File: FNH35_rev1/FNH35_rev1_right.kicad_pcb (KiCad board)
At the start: 2 copper layers, 126.2 x 116.7 mm, 117 parts, among them IC12 NUF2221W1T2G, J1 Conn_01x03, J2 Conn_01x08, J3 DX07B024JJ3R1600, K201 KEYSW, K202 KEYSW, K203 KEYSW, K204 KEYSW, K205 KEYSW, K206 KEYSW, K207 KEYSW, K208 KEYSW, K209 KEYSW, K210 KEYSW, K211 KEYSW, K212 KEYSW, K213 KEYSW, K214 KEYSW, K215 KEYSW, K216 KEYSW, K217 KEYSW, K218 KEYSW, SW1 SW_PUSH, U1 STM32F303CCTx, U2 LD1117S33TR_SOT223, U3 74AHCT125, X1 XTAL_GND

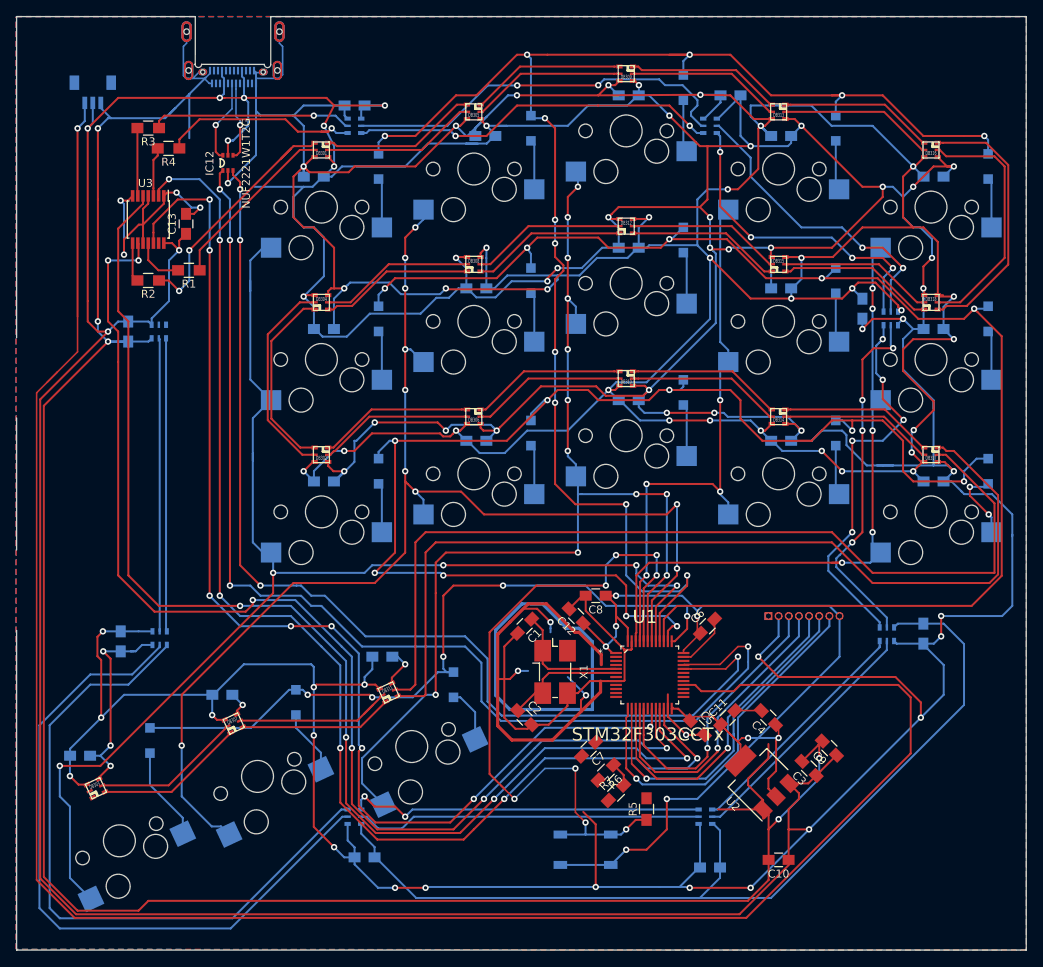
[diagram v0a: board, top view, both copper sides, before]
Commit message: GND and GNDD disconnected
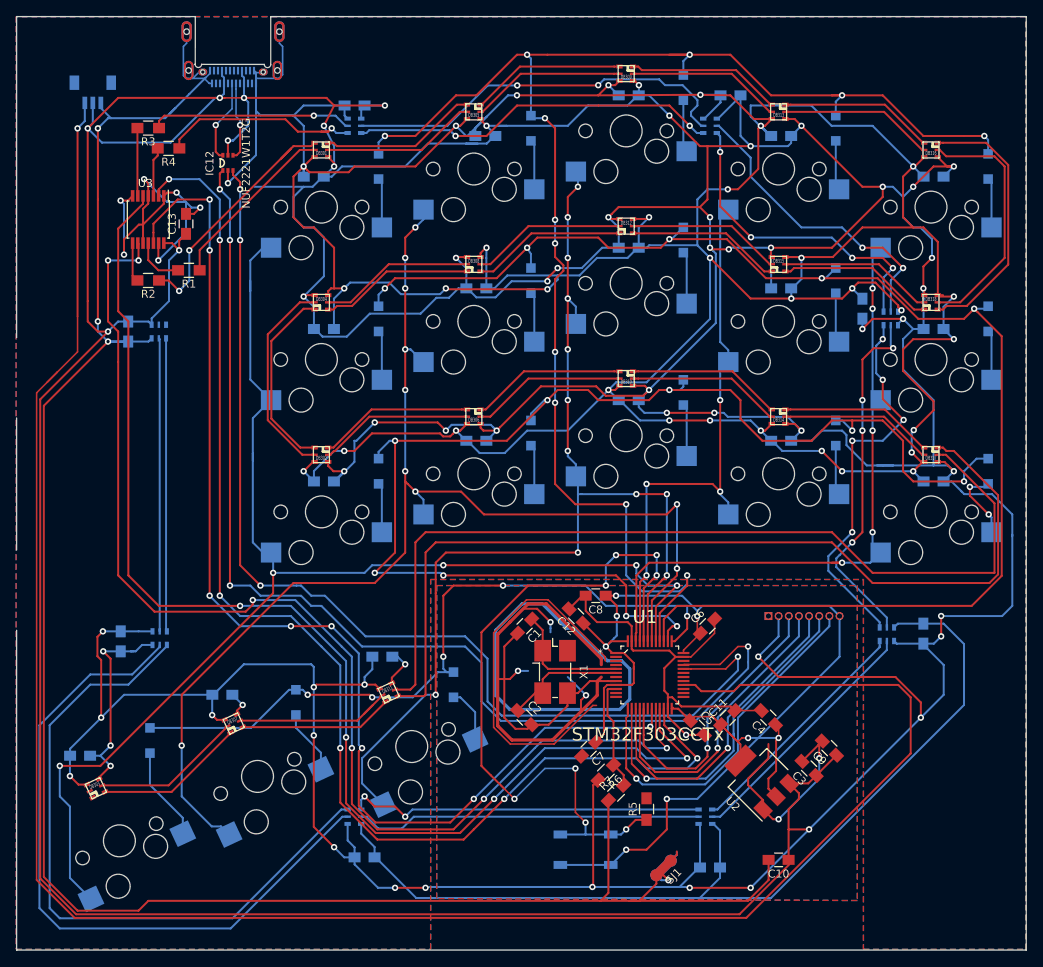
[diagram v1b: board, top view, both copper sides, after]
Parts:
- added SJ1: SOLDER_JUMPER, butts:gndcm, F.Cu at (220.9, 138.4)
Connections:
- C1 pad 2: GND -> GNDD
- C11 pad 2: GND -> GNDD
- C12 pad 2: GND -> GNDD
- C2 pad 2: GND -> GNDD
- C3 pad 2: GND -> GNDD
- C4 pad 2: GND -> GNDD
- C5 pad 2: GND -> GNDD
- C6 pad 2: GND -> GNDD
- C7 pad 2: GND -> GNDD
- C8 pad 2: GND -> GNDD
- C9 pad 2: GND -> GNDD
- R5 pad 2: GND -> GNDD
- U1 pad 23: GND -> GNDD
- U1 pad 35: GND -> GNDD
- U1 pad 47: GND -> GNDD
- U1 pad 8: GND -> GNDD
- U2 pad 1: GND -> GNDD
- X1 pad 3: GND -> GNDD
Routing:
- net GNDD: track 0.00 -> 179.1 mm, vias 0 -> 6
- net GND: track 1119.9 -> 984.3 mm, vias 51 -> 48
- net (no net): track 44.9 -> 98.1 mm
- net +5V: track 1058.7 -> 1081.9 mm
- net +3V3: track 142.1 -> 156.8 mm
- net /ADC: track 3.07 -> 13.9 mm
- net /BOOT: track 90.1 -> 91.5 mm
- added copper zone on B.Cu, net GNDD
- added copper zone on F.Cu, net GNDD
